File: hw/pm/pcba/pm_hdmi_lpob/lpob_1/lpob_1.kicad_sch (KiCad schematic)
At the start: 3 parts, among them J1 HDMI_A_1.4, J2 HDMI_A_1.4, J3 Conn_01x08_Pin

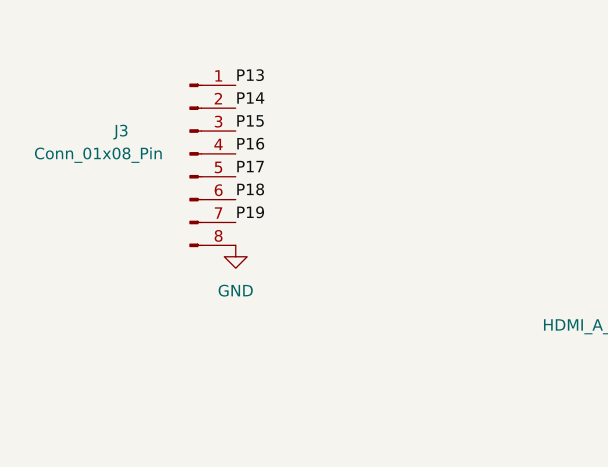
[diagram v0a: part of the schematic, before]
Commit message: 添加(pm/pcba): 生产 PCB JLC pm_hdmi_lpob v0.1 (2024-01-03)
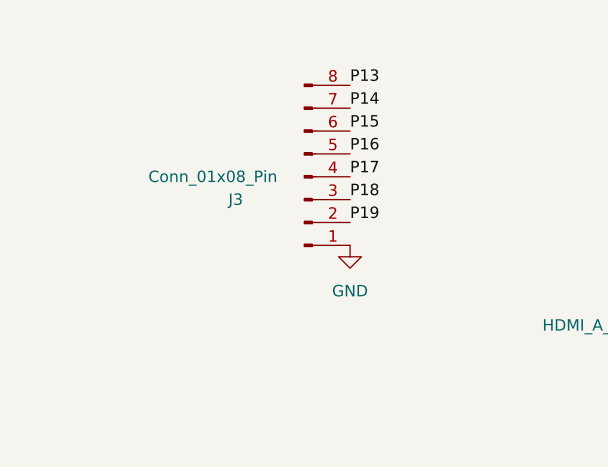
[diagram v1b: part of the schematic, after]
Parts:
- J1: footprint hdmi_a:hdmi_a_1 -> hdmi_a:hdmi_a_0
- J2: footprint hdmi_a:hdmi_a_2 -> hdmi_a:hdmi_a_1
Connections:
- net GND: now also J3.1 (Pin_1); no longer J3.8 (Pin_8)
- net P13: now also J3.8 (Pin_8); no longer J3.1 (Pin_1)
- net P14: now also J3.7 (Pin_7); no longer J3.2 (Pin_2)
- net P15: now also J3.6 (Pin_6); no longer J3.3 (Pin_3)
- net P16: now also J3.5 (Pin_5); no longer J3.4 (Pin_4)
- net P17: now also J3.4 (Pin_4); no longer J3.5 (Pin_5)
- net P18: now also J3.3 (Pin_3); no longer J3.6 (Pin_6)
- net P19: now also J3.2 (Pin_2); no longer J3.7 (Pin_7)
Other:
- moved on the sheet: J3
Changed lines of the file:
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@@
     (effects (font (size 1.27 1.27)) (justify left bottom))
   )
-  (label "P18" (at 152.4 50.8 0) (fields_autoplaced)
+  (label "P19" (at 165.1 53.34 0) (fields_autoplaced)
+    (effects (font (size 1.27 1.27)) (justify left bottom))
+  )
+  (label "P18" (at 165.1 50.8 0) (fields_autoplaced)
+    (effects (font (size 1.27 1.27)) (justify left bottom))
+  )
+  (label "P17" (at 165.1 48.26 0) (fields_autoplaced)
     (effects (font (size 1.27 1.27)) (justify left bottom))
   )
@@
     (effects (font (size 1.27 1.27)) (justify left bottom))
   )
-  (label "P19" (at 152.4 53.34 0) (fields_autoplaced)
+  (label "P13" (at 165.1 38.1 0) (fields_autoplaced)
     (effects (font (size 1.27 1.27)) (justify left bottom))
   )
@@
     (effects (font (size 1.27 1.27)) (justify left bottom))
   )
-  (label "P13" (at 152.4 38.1 0) (fields_autoplaced)
+  (label "P15" (at 165.1 43.18 0) (fields_autoplaced)
     (effects (font (size 1.27 1.27)) (justify left bottom))
   )
-  (label "P17" (at 152.4 48.26 0) (fields_autoplaced)
+  (label "P16" (at 165.1 45.72 0) (fields_autoplaced)
+    (effects (font (size 1.27 1.27)) (justify left bottom))
+  )
+  (label "P14" (at 165.1 40.64 0) (fields_autoplaced)
     (effects (font (size 1.27 1.27)) (justify left bottom))
   )
   (label "P19" (at 228.6 81.28 0) (fields_autoplaced)
-    (effects (font (size 1.27 1.27)) (justify left bottom))
-  )
-  (label "P16" (at 152.4 45.72 0) (fields_autoplaced)
-    (effects (font (size 1.27 1.27)) (justify left bottom))
-  )
-  (label "P14" (at 152.4 40.64 0) (fields_autoplaced)
     (effects (font (size 1.27 1.27)) (justify left bottom))
   )
@@
     (effects (font (size 1.27 1.27)) (justify left bottom))
   )
-  (label "P15" (at 152.4 43.18 0) (fields_autoplaced)
-    (effects (font (size 1.27 1.27)) (justify left bottom))
-  )
-  (symbol (lib_id "Connector:Conn_01x08_Pin") (at 147.32 45.72 0) (unit 1)
+  (symbol (lib_id "Connector:Conn_01x08_Pin") (at 160.02 48.26 0) (mirror x) (unit 1)
     (in_bom yes) (on_board yes) (dnp no)
-    (property "Reference" "J3" (at 139.7 43.18 0)
+    (property "Reference" "J3" (at 152.4 50.8 0)
       (effects (font (size 1.27 1.27)))
     )
-    (property "Value" "Conn_01x08_Pin" (at 137.16 45.72 0)
+    (property "Value" "Conn_01x08_Pin" (at 149.86 48.26 0)
       (effects (font (size 1.27 1.27)))
     )
-    (property "Footprint" "Connector_PinHeader_2.54mm:PinHeader_1x08_P2.54mm_Vertical" (at 147.32 45.72 0)
+    (property "Footprint" "Connector_PinHeader_2.54mm:PinHeader_1x08_P2.54mm_Vertical" (at 160.02 48.26 0)
       (effects (font (size 1.27 1.27)) hide)
     )
-    (property "Datasheet" "~" (at 147.32 45.72 0)
+    (property "Datasheet" "~" (at 160.02 48.26 0)
       (effects (font (size 1.27 1.27)) hide)
     )
@@
       (effects (font (size 1.27 1.27)) (justify left))
     )
-    (property "Footprint" "hdmi_a:hdmi_a_1" (at 249.555 63.5 0)
+    (property "Footprint" "hdmi_a:hdmi_a_0" (at 249.555 63.5 0)
       (effects (font (size 1.27 1.27)) hide)
     )
@@
       (effects (font (size 1.27 1.27)) (justify left))
     )
-    (property "Footprint" "hdmi_a:hdmi_a_2" (at 207.645 63.5 0)
+    (property "Footprint" "hdmi_a:hdmi_a_1" (at 207.645 63.5 0)
       (effects (font (size 1.27 1.27)) hide)
     )
@@
     )
   )
-  (symbol (lib_id "power:GND") (at 152.4 55.88 0) (unit 1)
+  (symbol (lib_id "power:GND") (at 165.1 55.88 0) (unit 1)
     (in_bom yes) (on_board yes) (dnp no) (fields_autoplaced)
-    (property "Reference" "#PWR02" (at 152.4 62.23 0)
+    (property "Reference" "#PWR02" (at 165.1 62.23 0)
       (effects (font (size 1.27 1.27)) hide)
     )
-    (property "Value" "GND" (at 152.4 60.96 0)
+    (property "Value" "GND" (at 165.1 60.96 0)
       (effects (font (size 1.27 1.27)))
     )
-    (property "Footprint" "" (at 152.4 55.88 0)
+    (property "Footprint" "" (at 165.1 55.88 0)
       (effects (font (size 1.27 1.27)) hide)
     )
-    (property "Datasheet" "" (at 152.4 55.88 0)
+    (property "Datasheet" "" (at 165.1 55.88 0)
       (effects (font (size 1.27 1.27)) hide)
     )
